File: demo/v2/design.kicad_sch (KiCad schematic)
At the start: 7 parts, among them J1 5V_IN, J2 3V3_OUT, U1 3.3V

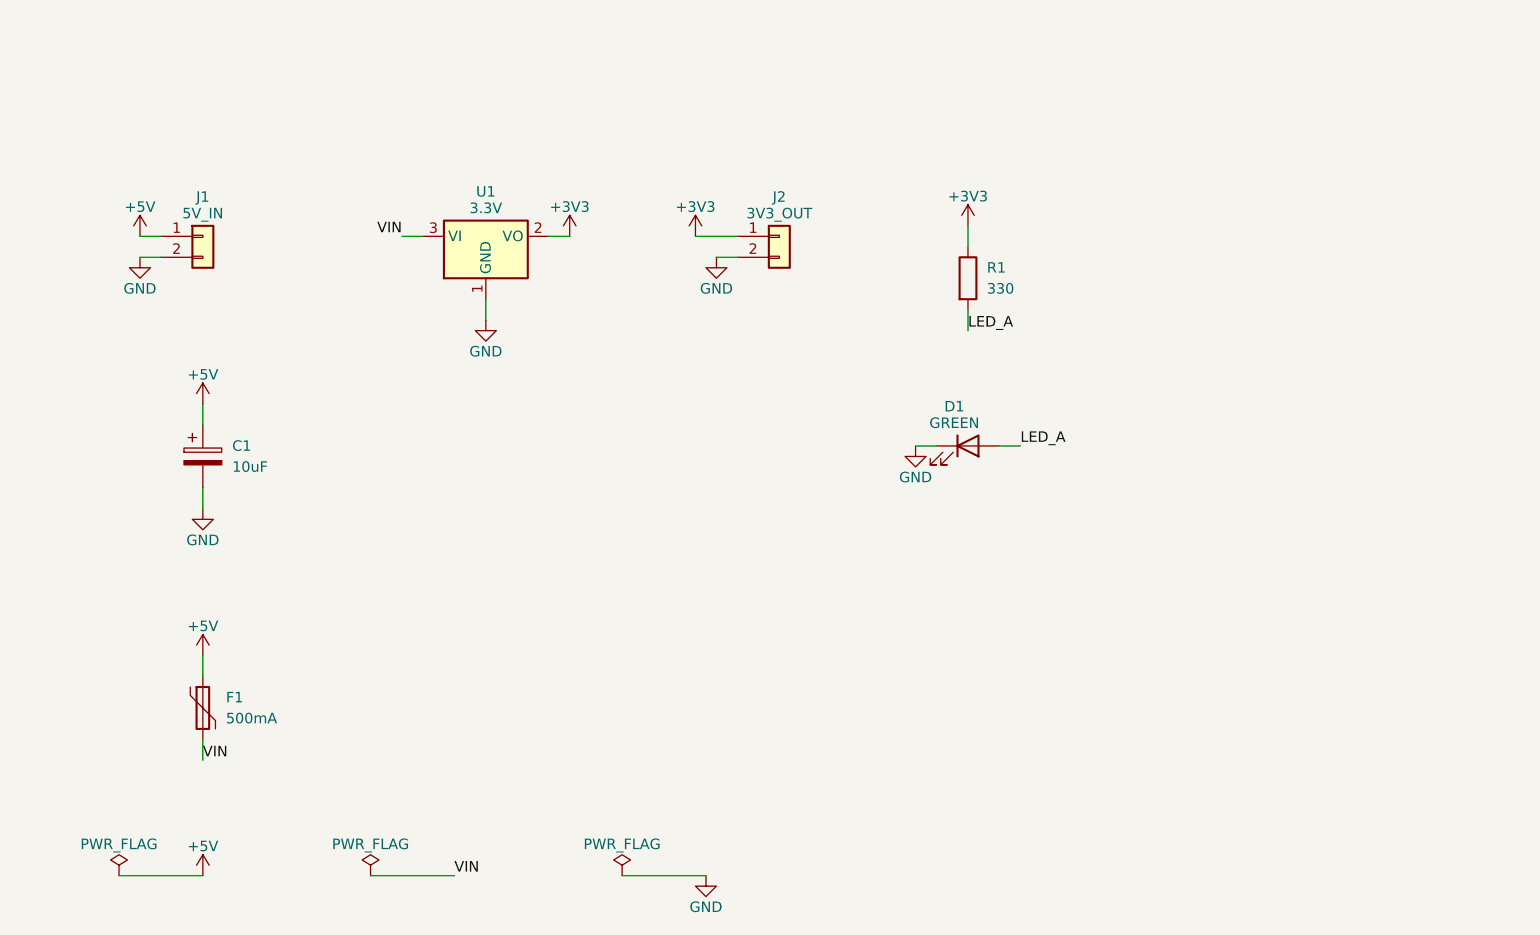
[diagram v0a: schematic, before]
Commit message: Draw schematics with routed wires; add MIC5317 and mounting-pin connector
Wired drafting is now the default: parts sit in a row on a common rail
line, a grid router draws each net as wires with junctions, each rail
gets one power symbol, and the sheet gets its title and a frame. A net
that cannot be routed falls back to the label style, which
hints.wiring "labels" also selects.

- lib/engine/wired.ts: row placement, connector mirroring, router,
  power-symbol and PWR_FLAG taps
- catalogue: Regulator_Linear:MIC5317-3.3xM5 and
  Connector_Generic_MountingPin:Conn_01x02_MountingPin; regulator
  rules accept VIN/VOUT pin names
- examples/mic5317-3v3.intent.json, with acceptance and engine tests
- studio: phone layout, 404 page, self-playing demo (?auto=1, ?start=N)
- demo and landing screenshot redrawn in the wired style
- eval re-run on the wired engine: 10/10 ERC-clean first time
- docs/LEARNINGS.md, docs/STACK.md, architecture diagram in README
- GitHub Actions workflow: type-check and build

Co-Authored-By: Claude Fable 5.1 <noreply@anthropic.com>
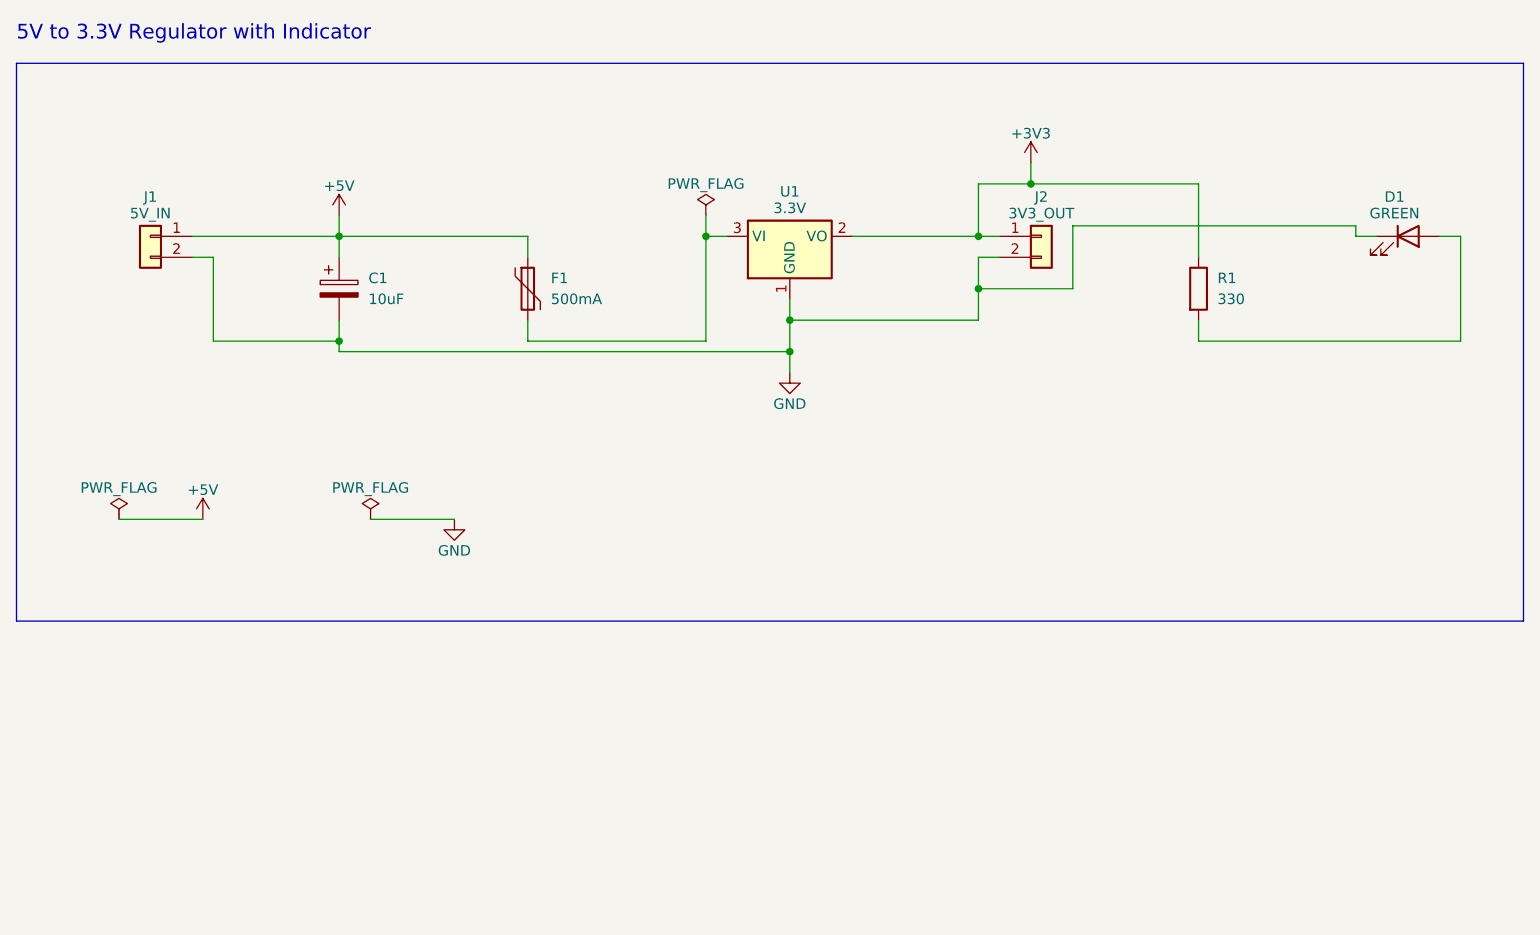
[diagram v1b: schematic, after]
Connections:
- net LED_A: no longer names the net of D1.2 (A), R1.2
- net VIN: no longer names the net of F1.2, U1.3 (VI)
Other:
- note added: "5V to 3.3V Regulator with Indicator"
- moved on the sheet: C1, D1, F1, J1, J2, R1, U1
